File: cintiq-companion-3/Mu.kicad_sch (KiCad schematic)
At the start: 12 parts, among them J1 Conn_01x03_Pin

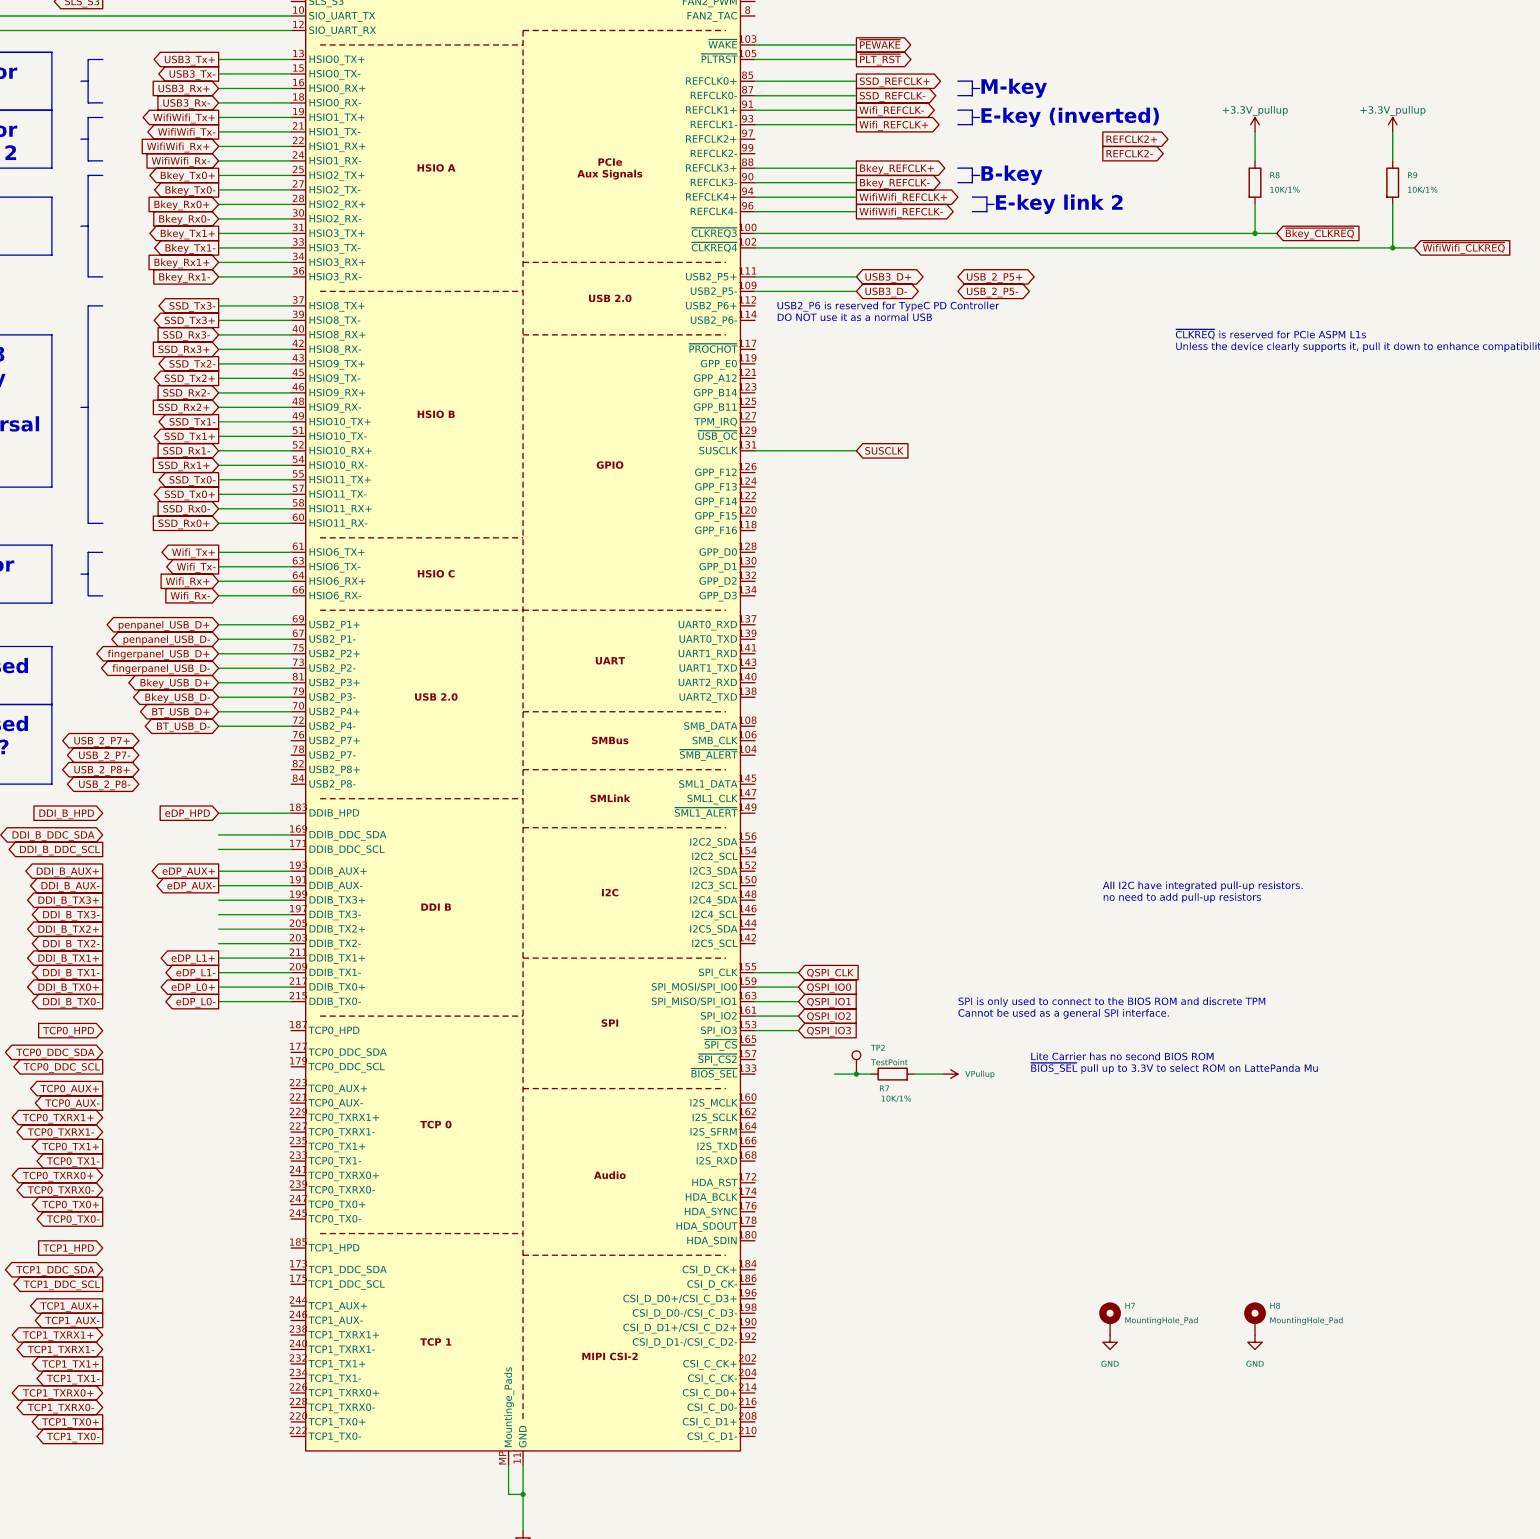
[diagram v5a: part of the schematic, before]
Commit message: Started adding type-c
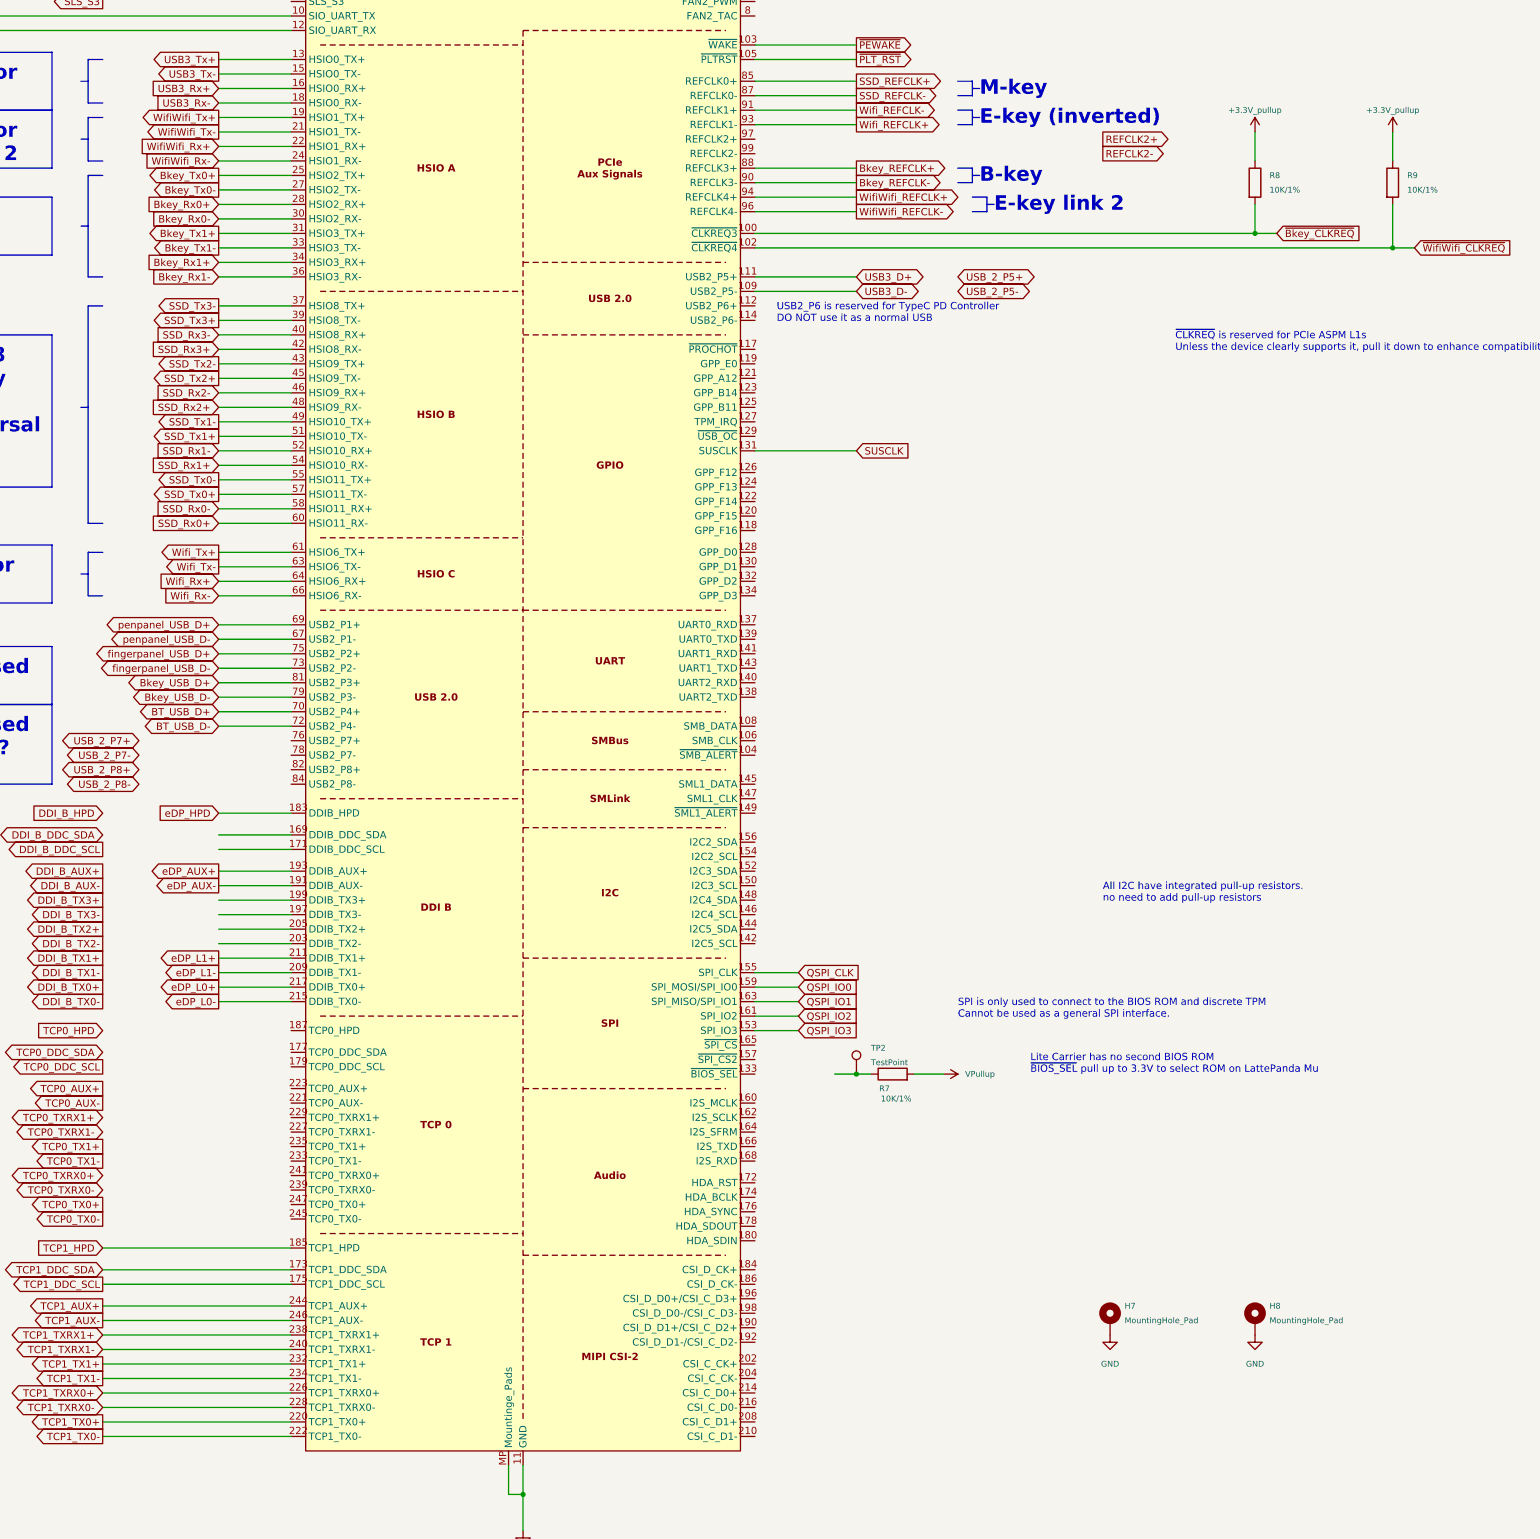
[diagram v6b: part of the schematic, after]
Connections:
- net TCP1_AUX+: now also A1.244 (TCP1_AUX+)
- net TCP1_AUX-: now also A1.246 (TCP1_AUX-)
- net TCP1_DDC_SCL: now also A1.175 (TCP1_DDC_SCL)
- net TCP1_DDC_SDA: now also A1.173 (TCP1_DDC_SDA)
- net TCP1_HPD: now also A1.185 (TCP1_HPD)
- net TCP1_TX0+: now also A1.220 (TCP1_TX0+)
- net TCP1_TX0-: now also A1.222 (TCP1_TX0-)
- net TCP1_TX1+: now also A1.232 (TCP1_TX1+)
- net TCP1_TX1-: now also A1.234 (TCP1_TX1-)
- net TCP1_TXRX0+: now also A1.226 (TCP1_TXRX0+)
- net TCP1_TXRX0-: now also A1.228 (TCP1_TXRX0-)
- net TCP1_TXRX1+: now also A1.238 (TCP1_TXRX1+)
- net TCP1_TXRX1-: now also A1.240 (TCP1_TXRX1-)
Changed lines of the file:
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@@
 		)
 	)
+	(wire
+		(pts
+			(xy 313.69 298.45) (xy 346.71 298.45)
+		)
+		(stroke
+			(width 0)
+			(type default)
+		)
+	)
 	(polyline
 		(pts
@@
 		)
 	)
+	(wire
+		(pts
+			(xy 313.69 318.77) (xy 346.71 318.77)
+		)
+		(stroke
+			(width 0)
+			(type default)
+		)
+	)
 	(polyline
 		(pts
@@
 	(wire
 		(pts
+			(xy 313.69 304.8) (xy 346.71 304.8)
+		)
+		(stroke
+			(width 0)
+			(type default)
+		)
+	)
+	(wire
+		(pts
 			(xy 334.01 228.6) (xy 346.71 228.6)
 		)
@@
 	(wire
 		(pts
+			(xy 313.69 331.47) (xy 346.71 331.47)
+		)
+		(stroke
+			(width 0)
+			(type default)
+		)
+	)
+	(wire
+		(pts
 			(xy 334.01 113.03) (xy 346.71 113.03)
 		)
@@
 	(wire
 		(pts
+			(xy 313.69 321.31) (xy 346.71 321.31)
+		)
+		(stroke
+			(width 0)
+			(type default)
+		)
+	)
+	(wire
+		(pts
 			(xy 334.01 201.93) (xy 346.71 201.93)
 		)
@@
 	(wire
 		(pts
+			(xy 313.69 308.61) (xy 346.71 308.61)
+		)
+		(stroke
+			(width 0)
+			(type default)
+		)
+	)
+	(wire
+		(pts
 			(xy 334.01 161.29) (xy 346.71 161.29)
 		)
@@
 	(wire
 		(pts
+			(xy 313.69 302.26) (xy 346.71 302.26)
+		)
+		(stroke
+			(width 0)
+			(type default)
+		)
+	)
+	(wire
+		(pts
 			(xy 387.35 341.63) (xy 387.35 347.98)
 		)
@@
 		)
 	)
+	(wire
+		(pts
+			(xy 313.69 313.69) (xy 346.71 313.69)
+		)
+		(stroke
+			(width 0)
+			(type default)
+		)
+	)
+	(wire
+		(pts
+			(xy 313.69 311.15) (xy 346.71 311.15)
+		)
+		(stroke
+			(width 0)
+			(type default)
+		)
+	)
 	(polyline
 		(pts
@@
 	(wire
 		(pts
+			(xy 313.69 326.39) (xy 346.71 326.39)
+		)
+		(stroke
+			(width 0)
+			(type default)
+		)
+	)
+	(wire
+		(pts
 			(xy 381 49.53) (xy 381 55.88)
 		)
@@
 	(wire
 		(pts
+			(xy 313.69 316.23) (xy 346.71 316.23)
+		)
+		(stroke
+			(width 0)
+			(type default)
+		)
+	)
+	(wire
+		(pts
 			(xy 515.62 120.65) (xy 519.43 120.65)
 		)
@@
 	(wire
 		(pts
+			(xy 313.69 323.85) (xy 346.71 323.85)
+		)
+		(stroke
+			(width 0)
+			(type default)
+		)
+	)
+	(wire
+		(pts
 			(xy 400.05 53.34) (xy 400.05 55.88)
 		)
@@
 	(wire
 		(pts
+			(xy 313.69 328.93) (xy 346.71 328.93)
+		)
+		(stroke
+			(width 0)
+			(type default)
+		)
+	)
+	(wire
+		(pts
 			(xy 334.01 179.07) (xy 346.71 179.07)
 		)
@@
 			(effects
 				(font
-					(size 1.27 1.27)
+					(size 1.016 1.016)
 				)
 				(hide yes)
@@
 			(effects
 				(font
-					(size 1.27 1.27)
+					(size 1.016 1.016)
 				)
 			)
@@
 			(effects
 				(font
-					(size 1.27 1.27)
+					(size 1.016 1.016)
 				)
 				(hide yes)
@@
 			(effects
 				(font
-					(size 1.27 1.27)
+					(size 1.016 1.016)
 				)
 			)
